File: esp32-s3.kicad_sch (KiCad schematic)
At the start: 14 parts, among them J3 Conn_01x05, SW1 RESET, SW2 BOOT, U3 ESP32-S3-WROOM-1

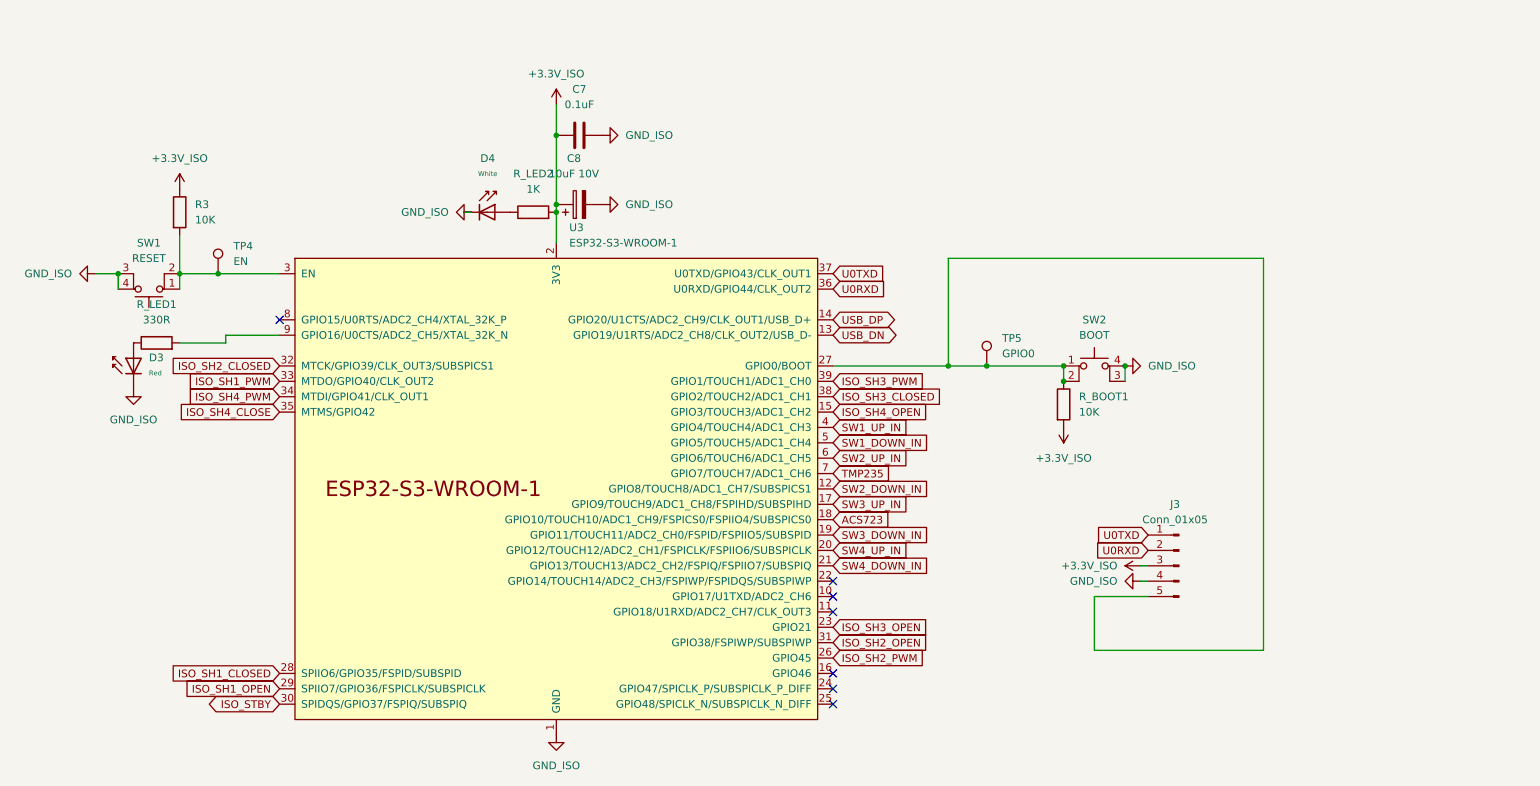
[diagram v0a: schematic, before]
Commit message: Completed added switch circuits
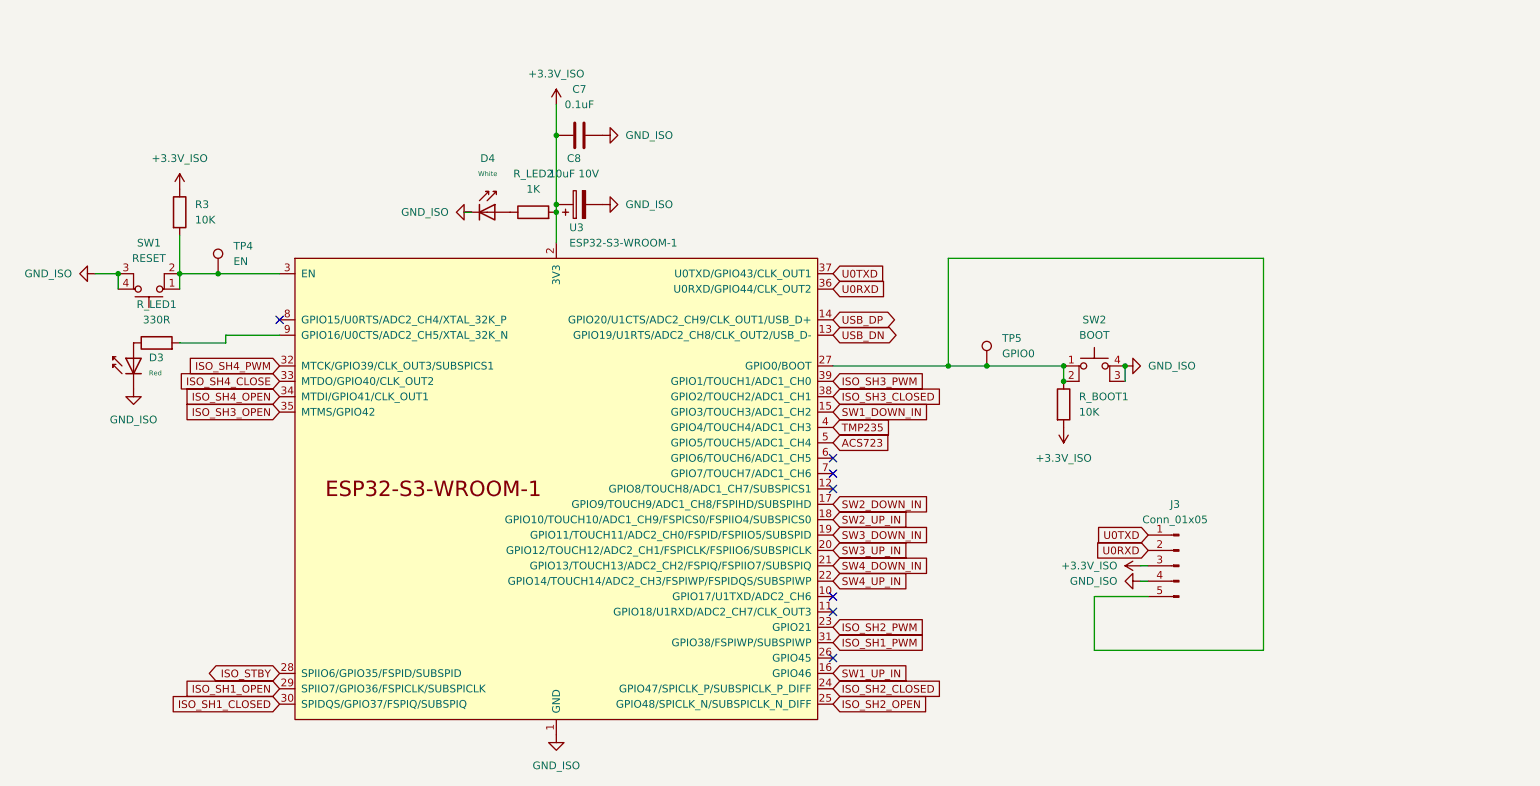
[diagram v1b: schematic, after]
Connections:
- net ACS723: now also U3.5 (GPIO5/TOUCH5/ADC1_CH4); no longer U3.18 (GPIO10/TOUCH10/ADC1_CH9/FSPICS0/FSPIIO4/SUBSPICS0)
- net ISO_SH1_CLOSED: now also U3.30 (SPIDQS/GPIO37/FSPIQ/SUBSPIQ); no longer U3.28 (SPIIO6/GPIO35/FSPID/SUBSPID)
- net ISO_SH1_PWM: now also U3.31 (GPIO38/FSPIWP/SUBSPIWP); no longer U3.33 (MTDO/GPIO40/CLK_OUT2)
- net ISO_SH2_CLOSED: now also U3.24 (GPIO47/SPICLK_P/SUBSPICLK_P_DIFF); no longer U3.32 (MTCK/GPIO39/CLK_OUT3/SUBSPICS1)
- net ISO_SH2_OPEN: now also U3.25 (GPIO48/SPICLK_N/SUBSPICLK_N_DIFF); no longer U3.31 (GPIO38/FSPIWP/SUBSPIWP)
- net ISO_SH2_PWM: now also U3.23 (GPIO21); no longer U3.26 (GPIO45)
- net ISO_SH3_OPEN: now also U3.35 (MTMS/GPIO42); no longer U3.23 (GPIO21)
- net ISO_SH4_CLOSE: now also U3.33 (MTDO/GPIO40/CLK_OUT2); no longer U3.35 (MTMS/GPIO42)
- net ISO_SH4_OPEN: now also U3.34 (MTDI/GPIO41/CLK_OUT1); no longer U3.15 (GPIO3/TOUCH3/ADC1_CH2)
- net ISO_SH4_PWM: now also U3.32 (MTCK/GPIO39/CLK_OUT3/SUBSPICS1); no longer U3.34 (MTDI/GPIO41/CLK_OUT1)
- net ISO_STBY: now also U3.28 (SPIIO6/GPIO35/FSPID/SUBSPID); no longer U3.30 (SPIDQS/GPIO37/FSPIQ/SUBSPIQ)
- net SW1_DOWN_IN: now also U3.15 (GPIO3/TOUCH3/ADC1_CH2); no longer U3.5 (GPIO5/TOUCH5/ADC1_CH4)
- net SW1_UP_IN: now also U3.16 (GPIO46); no longer U3.4 (GPIO4/TOUCH4/ADC1_CH3)
- net SW2_DOWN_IN: now also U3.17 (GPIO9/TOUCH9/ADC1_CH8/FSPIHD/SUBSPIHD); no longer U3.12 (GPIO8/TOUCH8/ADC1_CH7/SUBSPICS1)
- net SW2_UP_IN: now also U3.18 (GPIO10/TOUCH10/ADC1_CH9/FSPICS0/FSPIIO4/SUBSPICS0); no longer U3.6 (GPIO6/TOUCH6/ADC1_CH5)
- net SW3_UP_IN: now also U3.20 (GPIO12/TOUCH12/ADC2_CH1/FSPICLK/FSPIIO6/SUBSPICLK); no longer U3.17 (GPIO9/TOUCH9/ADC1_CH8/FSPIHD/SUBSPIHD)
- net SW4_UP_IN: now also U3.22 (GPIO14/TOUCH14/ADC2_CH3/FSPIWP/FSPIDQS/SUBSPIWP); no longer U3.20 (GPIO12/TOUCH12/ADC2_CH1/FSPICLK/FSPIIO6/SUBSPICLK)
- net TMP235: now also U3.4 (GPIO4/TOUCH4/ADC1_CH3); no longer U3.7 (GPIO7/TOUCH7/ADC1_CH6)

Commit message: Added RTS/DTS programing via UART circuitry, added LED control circuitry.
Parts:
- added C21: 1uF, Capacitor_SMD:C_0603_1608Metric, symbol Device:C
- added Q1: 2N7002, Package_TO_SOT_SMD:SOT-23, symbol Transistor_FET:2N7002
- added Q3, Q4: S8050, Package_TO_SOT_SMD:SOT-23, symbol Transistor_BJT:S8050
- added R18, R19, R20: 10K, Resistor_SMD:R_0603_1608Metric, symbol Device:R
- J3: value Conn_01x05 -> Conn_01x07; footprint Connector_PinHeader_2.54mm:PinHeader_1x05_P2.54mm_Vertical -> Connector_PinHeader_2.54mm:PinHeader_1x07_P2.54mm_Vertical; symbol Connector:Conn_01x05_Pin -> Connector:Conn_01x07_Pin
- U3: footprint Espressif:ESP32-S3-WROOM-1 -> PCM_Espressif:ESP32-S3-WROOM-1
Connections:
- net +3.3V_ISO: now also R18.1
- net GND_ISO: now also C21.2, Q1.2 (S); no longer D4.1
- net EN: now reaches R3.2, SW1.1, SW1.2, TP4.1, U3.3 (EN)
- net EN: now also C21.1, Q4.3 (C)
- net BOOT: now reaches J3.5 (Pin_5), R_BOOT1.1, SW2.1, SW2.2, TP5.1, U3.27 (GPIO0/BOOT)
- net BOOT: now also Q3.3 (C)
- net LED_D4_EN: now reaches U3.6 (GPIO6/TOUCH6/ADC1_CH5)
- net LED_D4_EN: now also Q1.1 (G), R18.2
- net LED_D5_CTRL: now reaches U3.7 (GPIO7/TOUCH7/ADC1_CH6)
- new net: Q3.2 (B), R19.1
- new net: Q4.2 (B), R20.2
- new net D4_CATHODE: D4.1, Q1.3 (D)
- new net DTR: J3.6 (Pin_6), Q3.1 (E), R20.1
- new net RTS: J3.7 (Pin_7), Q4.1 (E), R19.2
- no-connect marks 7 -> 5

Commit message: Update annotations, fixed font sizes.
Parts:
- renumbered C7 to C15, C8 to C16, C21 to C17, R3 to R11, R_BOOT1 to R12, R_LED1 to R13, R_LED2 to R14, R18 to R15, R19 to R18, R20 to R19
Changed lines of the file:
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@@
 		(dnp no)
 		(fields_autoplaced yes)
-		(property "Reference" "C7"
+		(property "Reference" "C15"
 			(at 118.11 26.67 90)
 			(show_name no)
@@
 			(project "barn-blinds-controller"
 				(path "/aa90962a-81b9-423d-8acd-c4e83fa798bb/3a264230-9604-4127-a232-ac76a818f339"
-					(reference "C7")
+					(reference "C15")
 					(unit 1)
 				)
@@
 		(dnp no)
 		(fields_autoplaced yes)
-		(property "Reference" "R_LED1"
+		(property "Reference" "R13"
 			(at 48.26 62.23 90)
 			(show_name no)
@@
 			(project "barn-blinds-controller"
 				(path "/aa90962a-81b9-423d-8acd-c4e83fa798bb/3a264230-9604-4127-a232-ac76a818f339"
-					(reference "R_LED1")
+					(reference "R13")
 					(unit 1)
 				)
@@
 		(dnp no)
 		(fields_autoplaced yes)
-		(property "Reference" "#PWR0119"
+		(property "Reference" "#PWR023"
 			(at 211.19 49.53 0)
 			(hide yes)
@@
 			(project "barn-blinds-controller"
 				(path "/aa90962a-81b9-423d-8acd-c4e83fa798bb/3a264230-9604-4127-a232-ac76a818f339"
-					(reference "#PWR0119")
+					(reference "#PWR023")
 					(unit 1)
 				)
@@
 		(dnp no)
 		(fields_autoplaced yes)
-		(property "Reference" "C8"
+		(property "Reference" "C16"
 			(at 117.221 38.1 90)
 			(show_name no)
@@
 			(project "barn-blinds-controller"
 				(path "/aa90962a-81b9-423d-8acd-c4e83fa798bb/3a264230-9604-4127-a232-ac76a818f339"
-					(reference "C8")
+					(reference "C16")
 					(unit 1)
 				)
@@
 		(dnp no)
 		(fields_autoplaced yes)
-		(property "Reference" "#PWR020"
+		(property "Reference" "#PWR019"
 			(at 128.27 45.72 0)
 			(hide yes)
@@
 			(project "barn-blinds-controller"
 				(path "/aa90962a-81b9-423d-8acd-c4e83fa798bb/3a264230-9604-4127-a232-ac76a818f339"
-					(reference "#PWR020")
+					(reference "#PWR019")
 					(unit 1)
 				)
@@
 		(dnp no)
 		(fields_autoplaced yes)
-		(property "Reference" "#PWR017"
+		(property "Reference" "#PWR016"
 			(at 114.3 33.02 0)
 			(hide yes)
@@
 			(project "barn-blinds-controller"
 				(path "/aa90962a-81b9-423d-8acd-c4e83fa798bb/3a264230-9604-4127-a232-ac76a818f339"
-					(reference "#PWR017")
+					(reference "#PWR016")
 					(unit 1)
 				)
@@
 		(dnp no)
 		(fields_autoplaced yes)
-		(property "Reference" "R_BOOT1"
+		(property "Reference" "R12"
 			(at 200.66 77.4699 0)
 			(show_name no)
@@
 			(project "barn-blinds-controller"
 				(path "/aa90962a-81b9-423d-8acd-c4e83fa798bb/3a264230-9604-4127-a232-ac76a818f339"
-					(reference "R_BOOT1")
+					(reference "R12")
 					(unit 1)
 				)
@@
 		(dnp no)
 		(fields_autoplaced yes)
-		(property "Reference" "#PWR018"
+		(property "Reference" "#PWR017"
 			(at 114.3 139.7 0)
 			(hide yes)
@@
 			(project "barn-blinds-controller"
 				(path "/aa90962a-81b9-423d-8acd-c4e83fa798bb/3a264230-9604-4127-a232-ac76a818f339"
-					(reference "#PWR018")
+					(reference "#PWR017")
 					(unit 1)
 				)
@@
 		(dnp no)
 		(fields_autoplaced yes)
-		(property "Reference" "#PWR0118"
+		(property "Reference" "#PWR020"
 			(at 188.65 16.24 0)
 			(hide yes)
@@
 			(project "barn-blinds-controller"
 				(path "/aa90962a-81b9-423d-8acd-c4e83fa798bb/3a264230-9604-4127-a232-ac76a818f339"
-					(reference "#PWR0118")
+					(reference "#PWR020")
 					(unit 1)
 				)
@@
 		(dnp no)
 		(fields_autoplaced yes)
-		(property "Reference" "#PWR019"
+		(property "Reference" "#PWR018"
 			(at 128.27 34.29 0)
 			(hide yes)
@@
 			(project "barn-blinds-controller"
 				(path "/aa90962a-81b9-423d-8acd-c4e83fa798bb/3a264230-9604-4127-a232-ac76a818f339"
-					(reference "#PWR019")
+					(reference "#PWR018")
 					(unit 1)
 				)
@@
 		(dnp no)
 		(fields_autoplaced yes)
-		(property "Reference" "#PWR024"
+		(property "Reference" "#PWR025"
 			(at 204.47 105.41 0)
 			(hide yes)
@@
 			(project "barn-blinds-controller"
 				(path "/aa90962a-81b9-423d-8acd-c4e83fa798bb/3a264230-9604-4127-a232-ac76a818f339"
-					(reference "#PWR024")
+					(reference "#PWR025")
 					(unit 1)
 				)
@@
 		(dnp no)
 		(fields_autoplaced yes)
-		(property "Reference" "R3"
+		(property "Reference" "R11"
 			(at 54.61 45.7199 0)
 			(show_name no)
@@
 			(project "barn-blinds-controller"
 				(path "/aa90962a-81b9-423d-8acd-c4e83fa798bb/3a264230-9604-4127-a232-ac76a818f339"
-					(reference "R3")
+					(reference "R11")
 					(unit 1)
 				)
@@
 		(dnp no)
 		(fields_autoplaced yes)
-		(property "Reference" "R18"
+		(property "Reference" "R15"
 			(at 191.19 28.97 0)
 			(show_name no)
@@
 			(project "barn-blinds-controller"
 				(path "/aa90962a-81b9-423d-8acd-c4e83fa798bb/3a264230-9604-4127-a232-ac76a818f339"
-					(reference "R18")
+					(reference "R15")
 					(unit 1)
 				)
@@
 		(dnp no)
 		(fields_autoplaced yes)
-		(property "Reference" "C21"
+		(property "Reference" "C17"
 			(at 266.7 36.83 0)
 			(show_name no)
@@
 			(project "barn-blinds-controller"
 				(path "/aa90962a-81b9-423d-8acd-c4e83fa798bb/3a264230-9604-4127-a232-ac76a818f339"
-					(reference "C21")
+					(reference "C17")
 					(unit 1)
 				)
@@
 		(dnp no)
 		(fields_autoplaced yes)
-		(property "Reference" "R19"
+		(property "Reference" "R18"
 			(at 243.84 31.75 90)
 			(show_name no)
@@
 			(project "barn-blinds-controller"
 				(path "/aa90962a-81b9-423d-8acd-c4e83fa798bb/3a264230-9604-4127-a232-ac76a818f339"
-					(reference "R19")
+					(reference "R18")
 					(unit 1)
 				)
@@
 		(dnp no)
 		(fields_autoplaced yes)
-		(property "Reference" "R_LED2"
+		(property "Reference" "R14"
 			(at 110.49 40.64 90)
 			(show_name no)
@@
 			(project "barn-blinds-controller"
 				(path "/aa90962a-81b9-423d-8acd-c4e83fa798bb/3a264230-9604-4127-a232-ac76a818f339"
-					(reference "R_LED2")
+					(reference "R14")
 					(unit 1)
 				)
@@
 		(dnp no)
 		(fields_autoplaced yes)
-		(property "Reference" "#PWR023"
+		(property "Reference" "#PWR024"
 			(at 214.63 102.87 0)
 			(hide yes)
@@
 			(project "barn-blinds-controller"
 				(path "/aa90962a-81b9-423d-8acd-c4e83fa798bb/3a264230-9604-4127-a232-ac76a818f339"
-					(reference "#PWR023")
+					(reference "#PWR024")
 					(unit 1)
 				)
@@
 		(dnp no)
 		(fields_autoplaced yes)
-		(property "Reference" "R20"
+		(property "Reference" "R19"
 			(at 247.65 71.12 90)
 			(show_name no)
@@
 			(project "barn-blinds-controller"
 				(path "/aa90962a-81b9-423d-8acd-c4e83fa798bb/3a264230-9604-4127-a232-ac76a818f339"
-					(reference "R20")
+					(reference "R19")
 					(unit 1)
 				)
@@
 		(dnp no)
 		(fields_autoplaced yes)
-		(property "Reference" "#PWR0122"
+		(property "Reference" "#PWR026"
 			(at 264.16 50.01 0)
 			(hide yes)
@@
 			(project "barn-blinds-controller"
 				(path "/aa90962a-81b9-423d-8acd-c4e83fa798bb/3a264230-9604-4127-a232-ac76a818f339"
-					(reference "#PWR0122")
+					(reference "#PWR026")
 					(unit 1)
 				)
